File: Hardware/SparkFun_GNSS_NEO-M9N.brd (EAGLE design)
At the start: 64.9 x 38 mm, 79 parts, among them J1 MICROMOD_STANDARD, J4 Bus Selection, U1 U-BLOX_NEO-M9N, U2 3.3V, U3 EEPROM, U4 74HC1G04

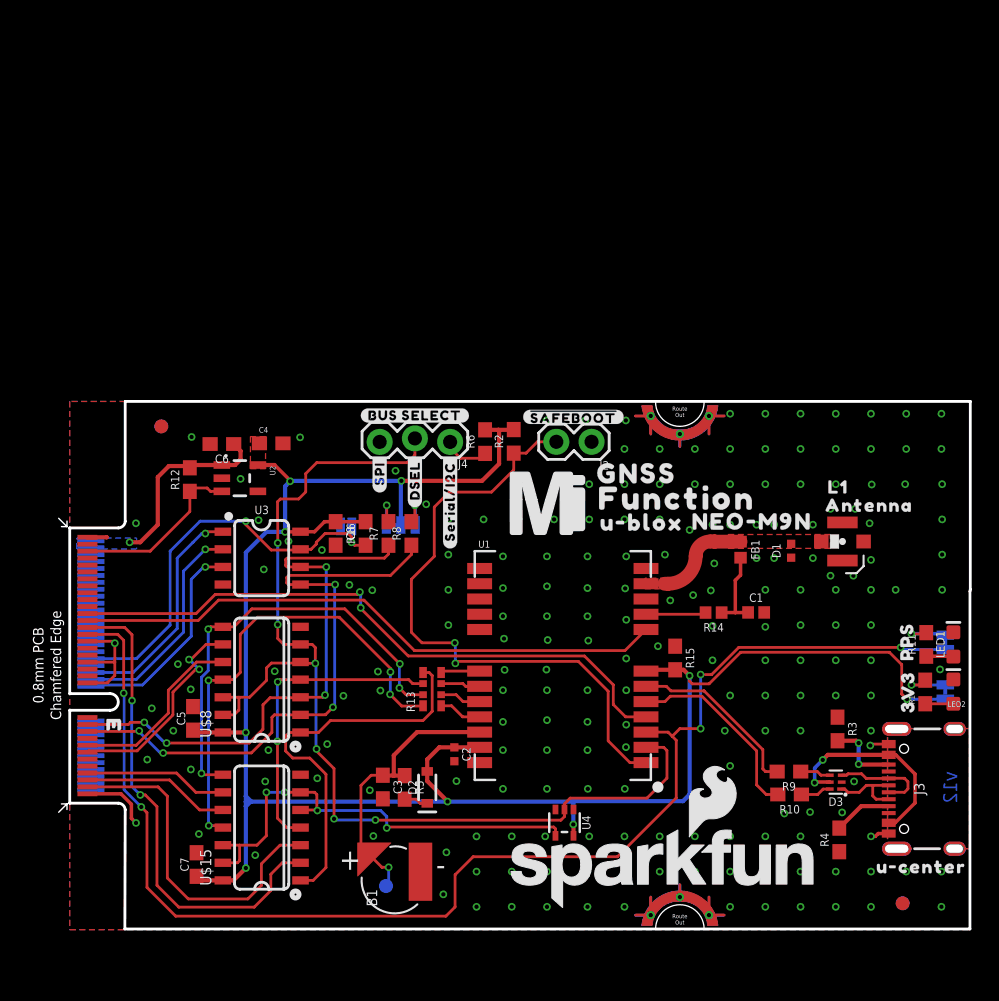
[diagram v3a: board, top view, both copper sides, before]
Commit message: Rotates board for paneling and corrected PCB edge
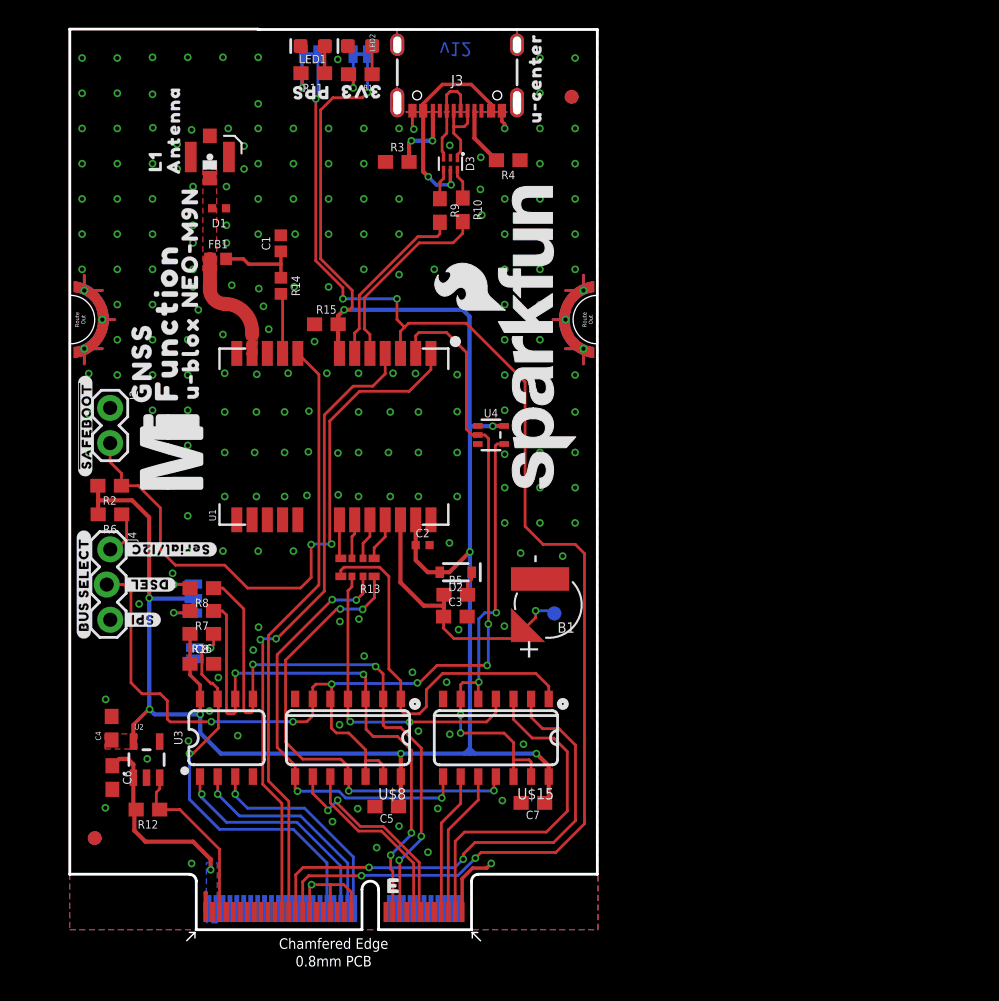
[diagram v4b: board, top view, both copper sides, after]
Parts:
- moved U$9 63.3 mm to (33.6, 61.4), turned to 90 degrees
- moved LED2 63.2 mm to (20.9, 63.7), turned to 180 degrees
- moved LED1 63.2 mm to (17.5, 63.7), turned to 180 degrees
- moved FD3 62.9 mm to (36.2, 60.1), turned to 270 degrees
- moved FD4 62.9 mm to (36.2, 60.1), turned to 90 degrees
- moved PWR\ 62.4 mm to (21.0, 63.1), turned to 180 degrees
- moved PPS 62.4 mm to (17.4, 63.1), turned to 180 degrees
- moved R11 60.5 mm to (17.5, 61.8), turned to 180 degrees
- moved R1 60.4 mm to (21.0, 61.7), turned to 180 degrees
- moved U$1 58.6 mm to (21.0, 60.5), turned to 180 degrees
- moved U$2 58.5 mm to (17.3, 60.4), turned to 180 degrees
- moved J3 57.5 mm to (27.9, 58.7), turned to 180 degrees
- moved U$12 57.4 mm to (21.0, 59.6), turned to 270 degrees
- moved U$13 57.3 mm to (17.4, 59.6), turned to 270 degrees
- moved U$7 57.0 mm to (7.49, 57.7), turned to 90 degrees
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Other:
- board size 64.9 x 38 mm -> 38 x 64.9 mm
- board text added: "0.8mm Thickness 45 degree chamfered edge ENIG Finish MicroMod"
- board text removed: "0.8mm PCB 45 degree chamfered edge ENIG Finish"

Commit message: Uses the updated function board outline
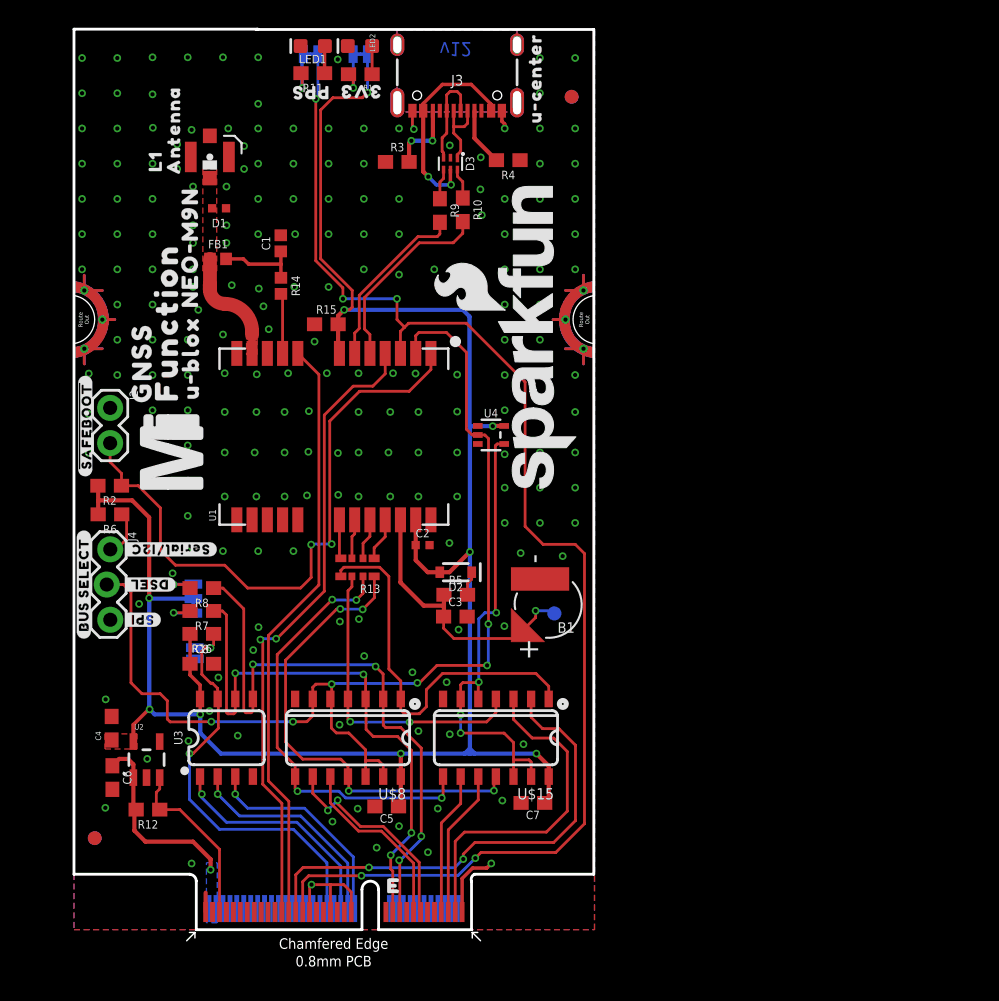
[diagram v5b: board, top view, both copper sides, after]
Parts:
- J1: value MICROMOD_STANDARD -> MICROMOD_FUNCTION_STANDARD; device SparkFun-MicroMod-Function:M.2-CARD-E-22_FUNCTION_STANDARD -> SparkFun-MicroMod:M.2-CARD-E-22_FUNCTION_STANDARD
- U1: device SparkFun-GPS:NEO-M9N/M8T/M8U -> SparkFun-GPS:NEO-M9N/M8T/M8U/D9S
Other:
- board size 38 x 64.9 mm -> 37.5 x 64.9 mm
